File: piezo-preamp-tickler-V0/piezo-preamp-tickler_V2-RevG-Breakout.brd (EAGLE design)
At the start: 88.3 x 60.3 mm, 67 parts, among them IC1 OPA2134UA, Q1 J201SOT-23, Q2 J201SOT-23, SW2-SPST INPUT-select

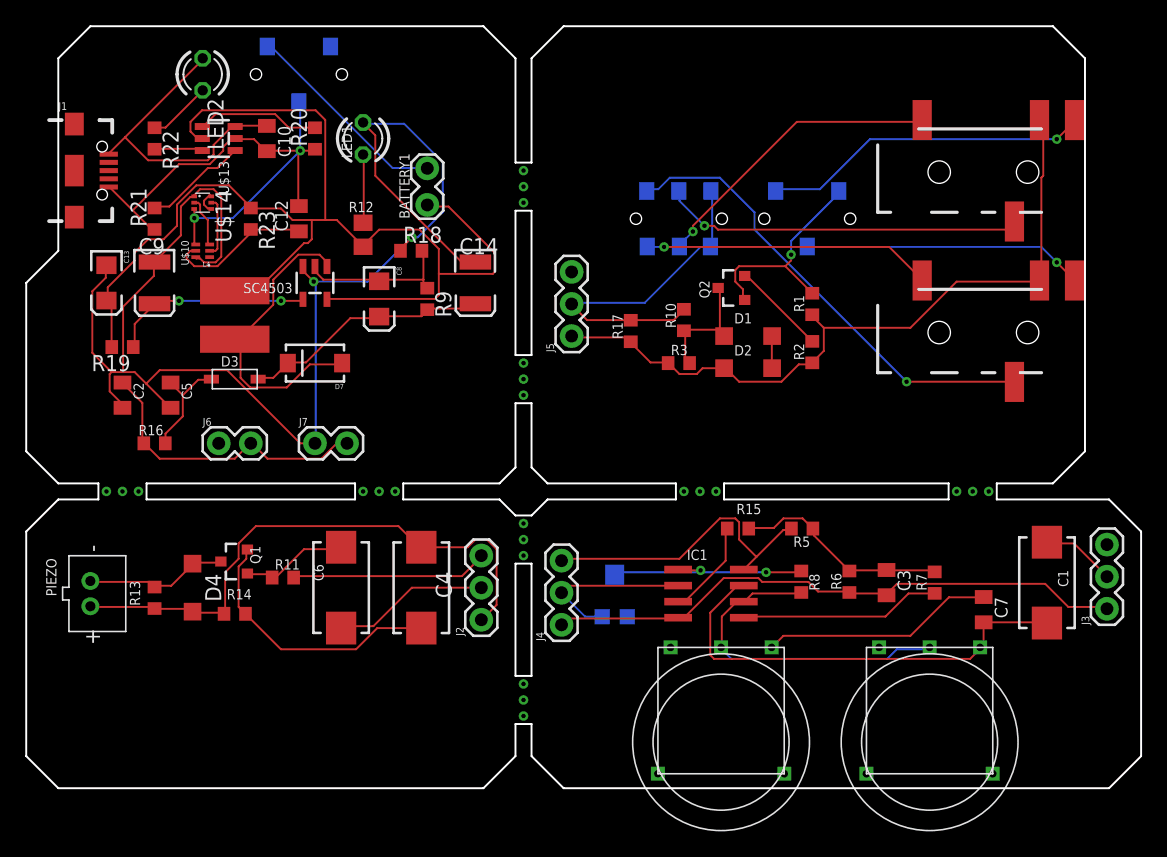
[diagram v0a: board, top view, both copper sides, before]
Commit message: updated footprints
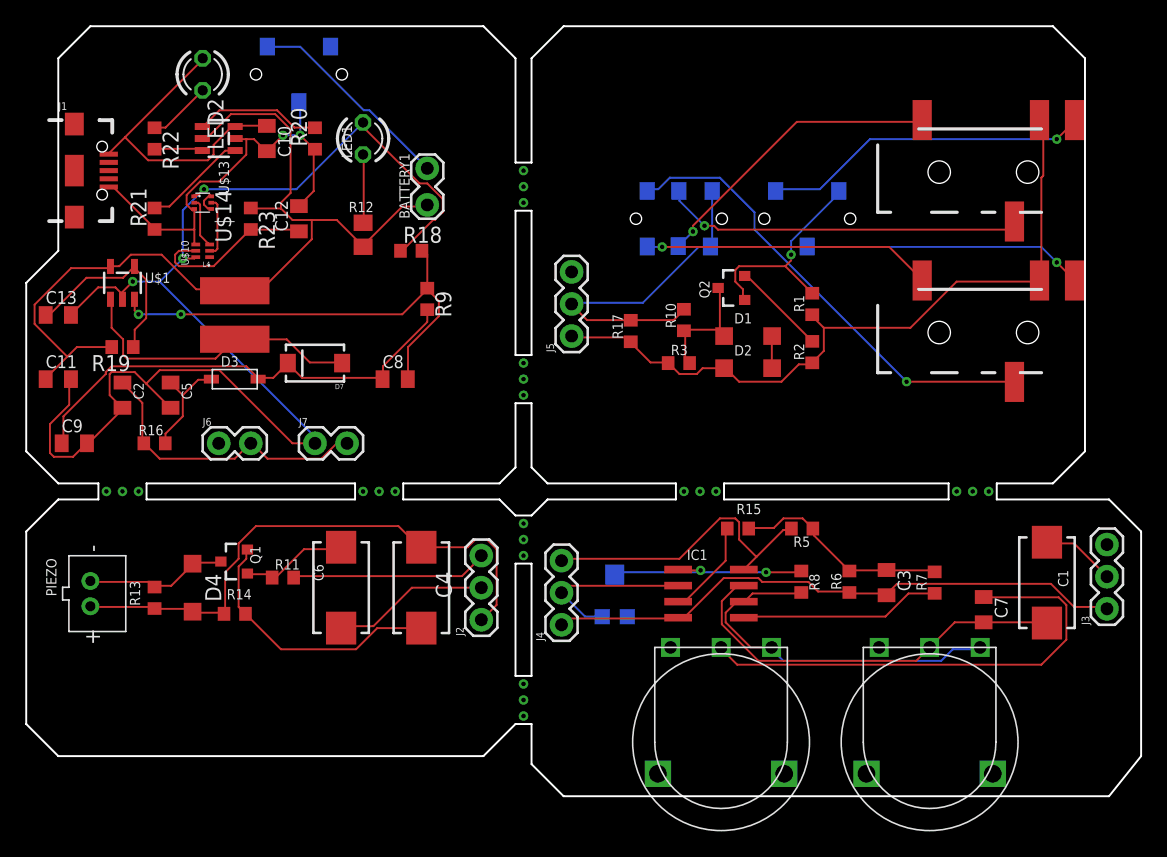
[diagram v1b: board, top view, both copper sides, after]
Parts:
- removed C14: 68uF, SparkFun:EIA3528
- removed SC4503: VREG12_SOT23-5, CMU-ArtFab:SOT23-5
- added C11: 10uF, adafruit:C0805K
- added U$1: SC4503, CMU-ArtFab:SOT23-5
- C13: value 10uF -> 0.1uF; device SparkFun:EIA3216 -> adafruit:C0805K
- C8: value 2.2pf -> 22pF; device SparkFun:EIA3216 -> adafruit:C0805K
- C9: value 56nf -> 10uF; device SparkFun:EIA3528 -> adafruit:C0805K
- U$2: device CMU-ArtFab:SWITCH_DPDT_CL-SB-12B -> CMU-ArtFab:SWITCH_DPDT_CL-SB-22B
- U$4, U$5: device CMU-ArtFab:THUMBPOT10MM -> CMU-ArtFab:THUMBPOT14
- moved C9 14.2 mm to (-12.7, -19.1), turned to 0 degrees
- moved C8 6.48 mm to (12.7, -14.0), turned to 0 degrees
- moved C13 4.58 mm to (-14.0, -8.89), turned to 0 degrees
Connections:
- net +12V: now also C8.1, C9.1; no longer C14.A, C8.A
- net GND: now also C11.2, C13.2, C9.2, U$1.2; no longer C13.C, C14.C, C9.C, SC4503.3
- net N$11: now also U$2.1, U$2.4; no longer U$2.P$1, U$2.P$6
- net N$13: now also U$2.2; no longer U$2.P$2
- net N$15: now also U$2.5; no longer U$2.P$5
- net N$26: now also U$2.6; no longer U$2.P$4
- net N$27: now also U$2.3; no longer U$2.P$3
- net N$29: now also C13.1, U$1.4; no longer C9.A, SC4503.4
- net N$30: now also C8.2, U$1.3; no longer C8.C, SC4503.2
- net N$32: now also U$1.1; no longer SC4503.1
- net VBAT: now also C11.1, U$1.5; no longer C13.A, SC4503.5
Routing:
- net VBAT: track 95.4 -> 71.1 mm
- net N$30: track 12.6 -> 36.8 mm, vias 0 -> 2
- net N$31: track 18.4 -> 38.3 mm
- net +12V: track 19.9 -> 37.7 mm
- net GND: track 116.5 -> 107.4 mm, vias 2 -> 3
- net GND1: track 44.2 -> 35.3 mm
- net N$6: track 36.0 -> 32.3 mm
- net N$7: track 26.9 -> 29.4 mm
- net N$34: track 11.8 -> 13.6 mm
- net N$32: track 24.8 -> 23.7 mm
- net N$29: track 16.1 -> 15.9 mm, vias 2 -> 0
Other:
- board size 88.3 x 60.3 mm -> 88.3 x 61 mm

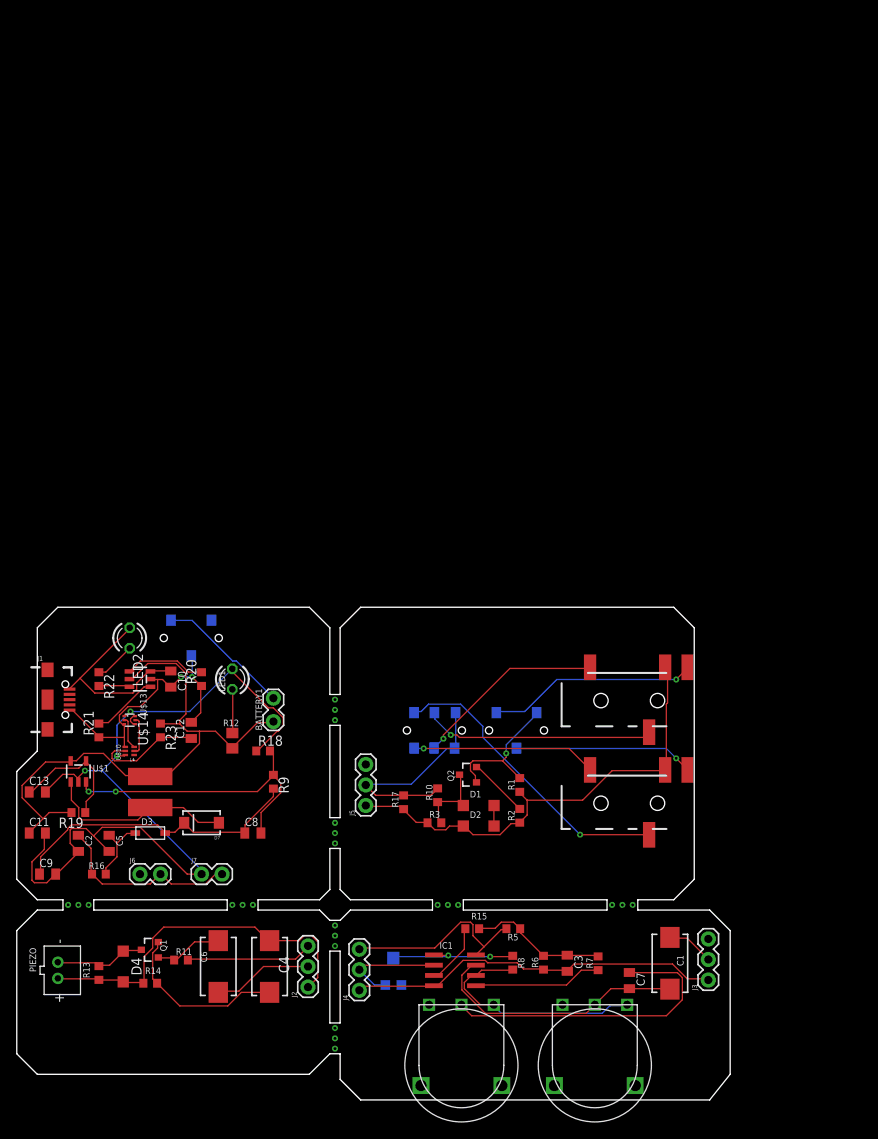
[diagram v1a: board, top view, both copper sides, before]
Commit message: changes to piezo-preamp-tickler_V2-RevG-Breakout -made all names/labels consistent in size/font and readable -moved all parts to top -rearranged (position and rotation) all components to mostly match the layout of the schematic for easier debugging -changed unnecessary 3-pin connectors to 2-pin -added independent 12V power inputs for buffer1 and buffer2 -label all connectors for inputs and outputs to subsystems make buffer1 and 2 identical, with optional caps and resistors -spread out all components as much as possible for easier debugging -added a bypass jumper to buffer to so we can totally disconnect/isolate buffer2 if we just want to list to the opamp output
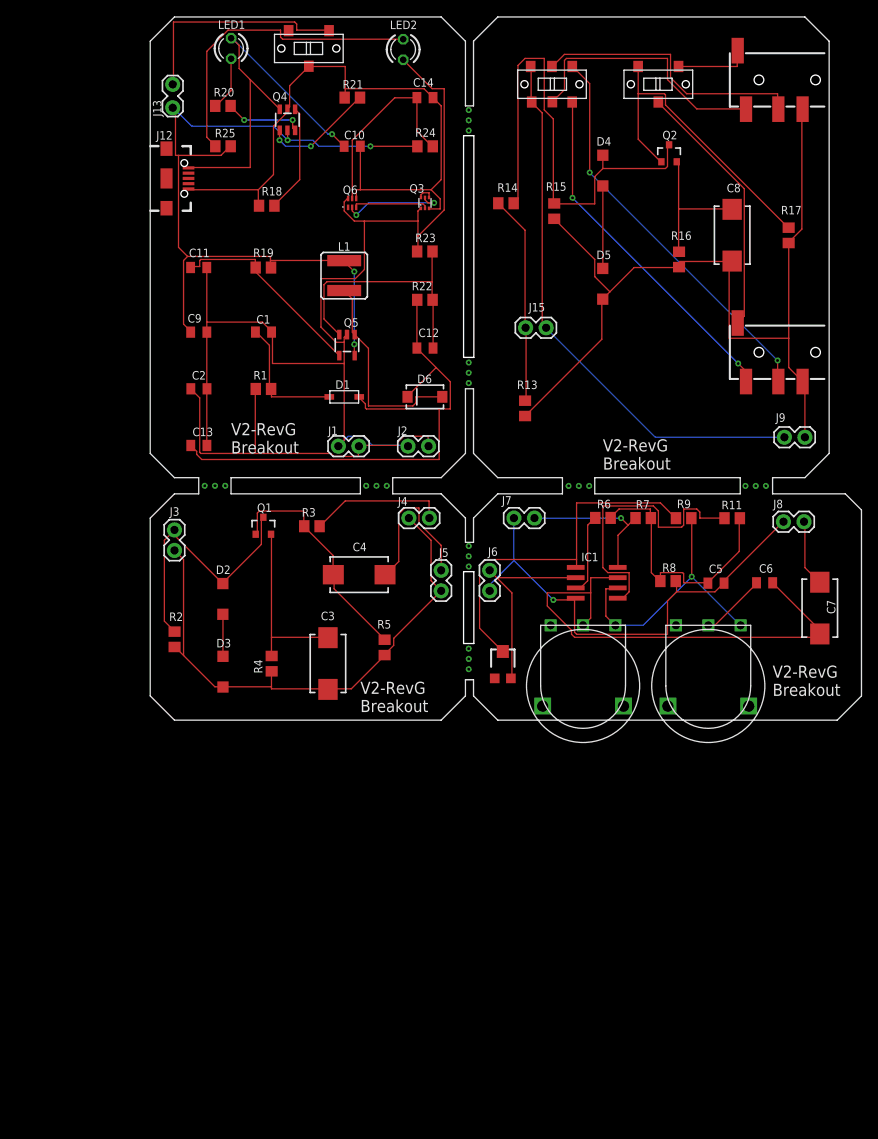
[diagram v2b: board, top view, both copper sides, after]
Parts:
- removed BATTERY1: (no value), SparkFun-Connectors:1X02_LOCK
- removed D7: 10BQ015, SparkFun:SMA-DIODE
- removed L4: 2.7uH, SparkFun:CR54
- removed PIEZO: (no value), adafruit:JST-PH-2-THM
- removed POWER: SPDT, CMU-ArtFab:SWITCH_SPDT_CL-SB-12B
- removed SW2-SPST: INPUT-select, CMU-ArtFab:SWITCH_SPDT_CL-SB-12B
- removed TO-HEADSET, TO-PHONE: AUDIO-JACK3LGPADS, Daniel:AUDIO-JACK-TRRS-SMD
- removed U$1: SC4503, CMU-ArtFab:SOT23-5
- removed U$10: BQ297X-BATTERY-MANAGER, CMU-ArtFab:WSON-6
- removed U$13: BQ21040-LIPO-CHARGER, CMU-ArtFab:SOT23-6
- removed U$14: DUAL-NFET-DMN2400, CMU-ArtFab:SOT-563
- removed U$2: SWITCH_DPDT, CMU-ArtFab:SWITCH_DPDT_CL-SB-22B
- removed U$4, U$5: (no value), CMU-ArtFab:THUMBPOT14
- added C14: 0.1uF, adafruit:C0805K
- added D5: MMSZ5231B, diode:SOD123
- added D6: 10BQ015, SparkFun:SMA-DIODE
- added J10, J11: AUDIO-JACK3LGPADS, Daniel:AUDIO-JACK-TRRS-SMD
- added J12: (no value), SparkFun-Connectors:USB-B-MICRO-SMD_RED_PASTE
- added J13: (no value), SparkFun-Connectors:1X02_LOCK
- added J15: Buf2_BYPASS, SparkFun-Connectors:1X02
- added J8: OpAmp_OUT, SparkFun-Connectors:1X02
- added J9: Buf2_IN, SparkFun-Connectors:1X02
- added L1: 2.7 uH, SparkFun-Coils:CR54
- added Q3: DMN2400, CMU-ArtFab:SOT-563
- added Q4: BQ21040, CMU-ArtFab:SOT23-6
- added Q5: SC4503, CMU-ArtFab:SOT23-5
- added Q6: BQ297X, CMU-ArtFab:WSON-6
- added R24: 330, CMU-ArtFab:R0805
- added R25: 390, CMU-ArtFab:R0805
- added SW1: SWITCH_DPDT, CMU-ArtFab:SWITCH_DPDT_CL-SB-22B
- added SW2: INPUT-select, CMU-ArtFab:SWITCH_SPDT_CL-SB-12B
- added SW3: SPDT, CMU-ArtFab:SWITCH_SPDT_CL-SB-12B
- added TM1: 20K, adafruit:TC33X
- C1: value 47uF -> 10uF; device adafruit:CT7343 -> adafruit:C0805K
- C11: value 10uF -> 0.1uF
- C12: value 0.1uF -> 22pF
- C13: value 0.1uF -> 10uF
- C3: value 10uF -> 150uF; device adafruit:C0805K -> adafruit:CT7343
- C4: value 150uF -> 3.3uF
- C6: value 3.3uF -> 10uF; device adafruit:CT7343 -> adafruit:C0805K
- C7: value 10uF -> 47uF; device adafruit:C0805K -> adafruit:CT7343
- C8: value 22pF -> 150uF; device adafruit:C0805K -> adafruit:CT7343
- D1: value (none) -> 1N4148; device diode:SOD123 -> adafruit:SOD-123
- D2, D4: value (none) -> MMSZ5231B
- D3: value 1N4148 -> MMSZ5231B; device adafruit:SOD-123 -> diode:SOD123
- J1: value (none) -> 12V; device SparkFun-Connectors:USB-B-MICRO-SMD_RED_PASTE -> SparkFun-Connectors:1X02
- J2, J4: value (none) -> 12V; device SparkFun-Connectors:1X03 -> SparkFun-Connectors:1X02
- J3: value (none) -> Piezo; device SparkFun-Connectors:1X03 -> SparkFun-Connectors:1X02
- J5: value (none) -> Buf1_OUT; device SparkFun-Connectors:1X03 -> SparkFun-Connectors:1X02
- J6: value (none) -> OpAmp_IN
- J7: value (none) -> 12V
- Q1: value J201SOT-23 -> J201
- R1: value 2.2K -> 10; device CMU-ArtFab:R0603 -> CMU-ArtFab:R0805
- R10: value 1K -> 10K; device CMU-ArtFab:R0603 -> CMU-ArtFab:THUMBPOT14
- R11: value 10K -> 1K; device CMU-ArtFab:R0603 -> CMU-ArtFab:R0805
- R12: value 390 -> 10K; device CMU-ArtFab:R0805 -> CMU-ArtFab:THUMBPOT14
- R13: value 10M -> 10K; device CMU-ArtFab:R0603 -> CMU-ArtFab:R0805
- R14: value 1.2K -> 1K; device CMU-ArtFab:R0603 -> CMU-ArtFab:R0805
- R15: value 1K -> 1M; device CMU-ArtFab:R0603 -> CMU-ArtFab:R0805
- R16: value 10 -> 1.2K; device CMU-ArtFab:R0603 -> CMU-ArtFab:R0805
- R17: value 10K -> 2.2K; device CMU-ArtFab:R0603 -> CMU-ArtFab:R0805
- R18: value 100k -> 10k; device CMU-ArtFab:R0603 -> CMU-ArtFab:R0805
- R19, R21: device CMU-ArtFab:R0603 -> CMU-ArtFab:R0805
- R2: value 1.2K -> 10M; device CMU-ArtFab:R0603 -> CMU-ArtFab:R0805
- R20: value 10k -> 1k; device CMU-ArtFab:R0603 -> CMU-ArtFab:R0805
- R22: value 1k -> 866k; device CMU-ArtFab:R0603 -> CMU-ArtFab:R0805
- R23: value 330 -> 100k; device CMU-ArtFab:R0603 -> CMU-ArtFab:R0805
- R3: value 1M -> 10K; device CMU-ArtFab:R0603 -> CMU-ArtFab:R0805
- R4: value 20K -> 1.2K; device adafruit:TC33X -> CMU-ArtFab:R0805
- R5: value 100K -> 2.2K; device CMU-ArtFab:R0603 -> CMU-ArtFab:R0805
- R6: value 150K -> 1K; device CMU-ArtFab:R0603 -> CMU-ArtFab:R0805
- R7: value 1K -> 100K; device CMU-ArtFab:R0603 -> CMU-ArtFab:R0805
- R8: value 1K -> 150K; device CMU-ArtFab:R0603 -> CMU-ArtFab:R0805
- R9: value 866k -> 1K; device CMU-ArtFab:R0603 -> CMU-ArtFab:R0805
- moved D4 115.0 mm to (56.0, 68.0)
- moved R14 106.1 mm to (44.0, 64.0), turned to 180 degrees
- moved R16 104.6 mm to (65.4, 57.0), turned to 90 degrees
- moved C8 94.8 mm to (72.0, 60.0), turned to 90 degrees
- moved C1 92.9 mm to (14.0, 48.0), turned to 0 degrees
- moved R15 89.4 mm to (50.0, 63.0), turned to 90 degrees
- moved R13 87.5 mm to (46.4, 38.6)
- moved R11 87.4 mm to (72.0, 25.0)
- moved R17 84.8 mm to (79.0, 60.0)
- moved J3 84.8 mm to (3.00, 21.0)
- moved R21 84.3 mm to (25.0, 77.0), turned to 0 degrees
- moved C6 82.6 mm to (76.0, 17.0), turned to 0 degrees
- moved C5 81.7 mm to (70.0, 16.9), turned to 0 degrees
- moved Q2 80.7 mm to (64.2, 70.1), turned to 0 degrees
- moved LED2 80.3 mm to (31.3, 83.0)
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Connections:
- removed net N$47: C3.2, IC1.4, J3.1, J4.1, R6.1
- new net N$20: C3.-, D3.C, J3.1, J4.1, J5.1, R2.1, R4.1, R5.1
- new net N$46: J15.2, R13.2, R14.2
- new net N$8: D2.A, D3.A
- net +12V: now also C12.1, C13.1, D1.A, D6.C, R22.2; no longer C8.1, C9.1, D3.A, D7.C, R9.2
- net GND: now also C1.2, J1.1, J2.1, LED2.K, Q3.1, Q5.2, Q6.6, R23.1; no longer C5.2, J7.1, LED1.K, R18.1, U$1.2, U$10.6, U$14.1
- net GND1: now also C14.2, J12.GND, Q3.3, Q4.5, Q6.4, R18.1, SW3.P$2; no longer C12.2, J1.GND, POWER.P$2, R20.1, U$10.4, U$13.5, U$14.3
- net N$1: now also D4.A, D5.A; no longer D1.A, D2.A
- net N$10: now also D4.C, R14.1, R15.2; no longer D1.C, R10.1, R3.2
- net N$11: now also J15.1, J9.2, SW1.1, SW1.4; no longer J5.2, R10.2, R17.2, U$2.1, U$2.4
- net N$12: now also J10.EARTH, SW2.P$1; no longer SW2-SPST.P$1, TO-HEADSET.EARTH
- net N$13: now also J10.TIP, SW1.2; no longer TO-HEADSET.TIP, U$2.2
- net N$14: now also C3.+, R4.2; no longer C4.+, R14.2
- net N$15: now also J10.RING1, SW1.5; no longer TO-HEADSET.RING1, U$2.5
- net N$16: now also C1.1, D1.C, R1.2; no longer C5.1, D3.C, R16.2
- net N$17: now also J11.EARTH, SW2.P$2; no longer SW2-SPST.P$2, TO-PHONE.EARTH
- net N$18: now also LED2.A, R25.1; no longer LED1.A, R12.1
- net N$19: now also J6.2, TM1.3; no longer J4.2, R4.3
- net N$2: now also D2.C, J3.2, R2.2; no longer D4.C, PIEZO.2, R13.2
- net N$21: now also J13.2, SW3.P$1; no longer BATTERY1.2, POWER.P$1
- net N$22: now also R6.1; no longer R15.1
- net N$23: now also C5.1, R11.2, R7.1, R8.2; no longer C3.1, R15.2, R5.1, R7.2
- net N$24: now also R9.1, TM1.2; no longer R4.2, R8.1
- net N$25: now also J4.2, R3.2; no longer J2.3, R11.2
- net N$26: now also J11.RING1, SW1.6; no longer TO-PHONE.RING1, U$2.6
- net N$27: now also J11.TIP, SW1.3; no longer TO-PHONE.TIP, U$2.3
- net N$28: now also C4.-, J5.2; no longer C6.-, J2.2
- net N$29: now also C11.1, Q5.4; no longer C13.1, U$1.4
- net N$3: now also C8.+, R16.2; no longer R2.2
- net N$30: now also C12.2, Q5.3, R22.1, R23.2; no longer C8.2, R18.2, R9.1, U$1.3
- net N$31: now also C6.1, R12.P$2; no longer C7.1, U$5.P$2
- net N$32: now also D6.A, L1.P$2, Q5.1; no longer D7.A, L4.P$2, U$1.1
- net N$33: now also Q4.3, R20.2; no longer R22.2, U$13.3
- net N$34: now also C14.1, Q6.5, R24.2; no longer C12.1, R23.2, U$10.5
- net N$35: now also Q4.1, R21.2; no longer R20.2, U$13.1
- net N$36: now also C7.-, J8.2; no longer C1.-, J3.2
- net N$37: now also Q3.4, Q3.6; no longer U$14.4, U$14.6
- net N$38: now also Q4.4, R18.2; no longer R21.2, U$13.4
- net N$39: now also Q3.5, Q6.2; no longer U$10.2, U$14.5
- net N$40: now also LED1.K, R20.1; no longer LED2.K, R22.1
- net N$41: now also Q3.2, Q6.3; no longer U$10.3, U$14.2
- net N$42: now also J7.2, R7.2; no longer J4.3, R5.2
- net N$43: now also J1.2, J2.2, R1.1; no longer J6.2, J7.2, R16.1
- net N$44: now also C5.2, IC1.4, J6.1, J7.1, J8.1, R8.1; no longer C4.-, D4.A, J2.1, PIEZO.1, R13.1, R14.1
- net N$45: now also C8.-, D5.C, J10.RING2, J11.RING2, J9.1, R13.1, R15.1, R16.1; no longer D2.C, J5.1, R1.1, R2.1, R3.1, TO-HEADSET.RING2, TO-PHONE.RING2
- net N$5: now also R11.1; no longer R7.1
- net N$6: now also C6.2, C7.+, R10.P$2; no longer C1.+, C7.2, U$4.P$2
- net N$7: now also R10.P$1, R12.P$1, R9.2; no longer R8.2, U$4.P$1, U$5.P$1
- net N$9: now also C4.+, R3.1, R5.2; no longer C6.+, R11.1
- net SELECT: now also R17.2, SW2.P$3; no longer R1.2, SW2-SPST.P$3
- net V+: now also J12.VBUS, LED1.A, Q4.6; no longer J1.VBUS, LED2.A, U$13.6
- net VBAT: now also C9.1, J13.1, L1.P$1, Q4.2, Q5.5, R24.1, R25.2; no longer BATTERY1.1, C11.1, L4.P$1, R12.2, R23.1, U$1.5, U$13.2
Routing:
- net N$20: track 0.00 -> 67.0 mm
- net N$10: track 10.2 -> 61.7 mm
- net N$45: track 57.9 -> 108.1 mm
- net N$47: track 46.6 -> 0.00 mm
- net GND1: track 35.3 -> 80.6 mm, vias 2 -> 0
- net N$11: track 27.2 -> 68.3 mm
- net N$18: track 5.47 -> 38.5 mm
- net +12V: track 37.7 -> 70.5 mm
- net VBAT: track 71.1 -> 102.9 mm, vias 0 -> 4
- net N$31: track 38.3 -> 8.20 mm
- net N$6: track 32.3 -> 61.4 mm
- net N$24: track 16.9 -> 45.2 mm, vias 2 -> 0
- net N$46: track 0.00 -> 25.9 mm
- net V+: track 24.4 -> 49.4 mm, vias 0 -> 1
- net GND: track 107.4 -> 132.1 mm, vias 3 -> 0
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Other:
- board size 88.3 x 61 mm -> 1.3 x 67.3 mm
- board text added: "V2-RevG Breakout"
